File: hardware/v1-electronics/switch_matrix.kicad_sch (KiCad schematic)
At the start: 230 parts, among them SW1 MSwitch, SW10 MSwitch, SW11 MSwitch, SW12 MSwitch, SW13 MSwitch, SW14 MSwitch, SW15 MSwitch, SW16 MSwitch, SW17 MSwitch, SW18 MSwitch, SW19 MSwitch, SW2 MSwitch, SW20 MSwitch, SW21 SW_DIP_x01, SW22 SW_DIP_x01, SW23 MSwitch, SW24 MSwitch, SW25 MSwitch, SW26 MSwitch, SW27 MSwitch, SW28 MSwitch, SW29 MSwitch, SW3 MSwitch, SW30 MSwitch, SW31 MSwitch, SW32 MSwitch, SW33 MSwitch, SW34 MSwitch, SW35 SW_DIP_x01, SW36 SW_DIP_x01, SW37 MSwitch, SW38 MSwitch, SW39 MSwitch, SW4 MSwitch, SW40 MSwitch, SW41 MSwitch, SW42 MSwitch, SW43 MSwitch, SW44 MSwitch, SW45 MSwitch, SW46 MSwitch, SW47 MSwitch, SW48 MSwitch, SW49 SW_DIP_x01, SW5 MSwitch, SW50 SW_DIP_x01, SW51 MSwitch, SW52 MSwitch, SW53 MSwitch, SW54 MSwitch, SW55 MSwitch, SW56 MSwitch, SW57 MSwitch, SW58 MSwitch, SW59 MSwitch, SW6 MSwitch, SW60 MSwitch, SW61 MSwitch, SW62 MSwitch, SW63 SW_Push, SW64 SW_DIP_x01, SW65 SW_DIP_x01, SW66 SW_Push, SW67 MSwitch, SW68 MSwitch, SW69 MSwitch, SW7 SW_DIP_x01, SW70 MSwitch, SW71 MSwitch, SW72 MSwitch, SW73 SW_DIP_x01, SW74 SW_DIP_x01, SW75 SW_DIP_x01, SW76 SW_DIP_x01, SW8 SW_DIP_x01, SW9 MSwitch

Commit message: refactor(v1 hardware): root level schematic is made discriptive with hierarchical pins
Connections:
- net Column 1 renamed Column1
- net Column 10 renamed Column10
- net Column 11 renamed Column11
- net Column 12 renamed Column12
- net Column 13 renamed Column13
- net Column 14 renamed Column14
- net Column 2 renamed Column2
- net Column 3 renamed Column3
- net Column 4 renamed Column4
- net Column 5 renamed Column5
- net Column 6 renamed Column6
- net Column 7 renamed Column7
- net Column 8 renamed Column8
- net Column 9 renamed Column9
- net Row 1 renamed Row1
- net Row 2 renamed Row2
- net Row 3 renamed Row3
- net Row 4 renamed Row4
- net Row 5 renamed Row5
- net Row 6 renamed Row6

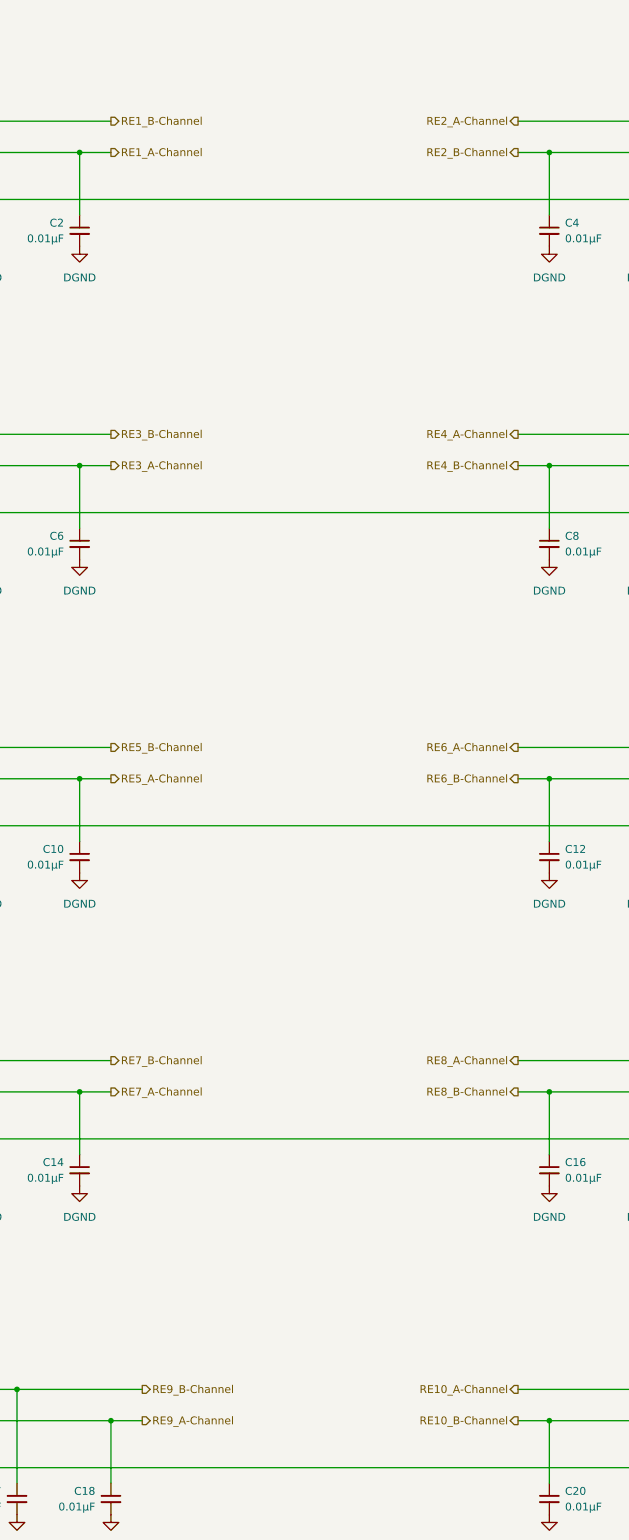
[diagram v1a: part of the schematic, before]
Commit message: refactor(v1 hardware): transition to hierarchical pins complete
All the buses renamed to stuff
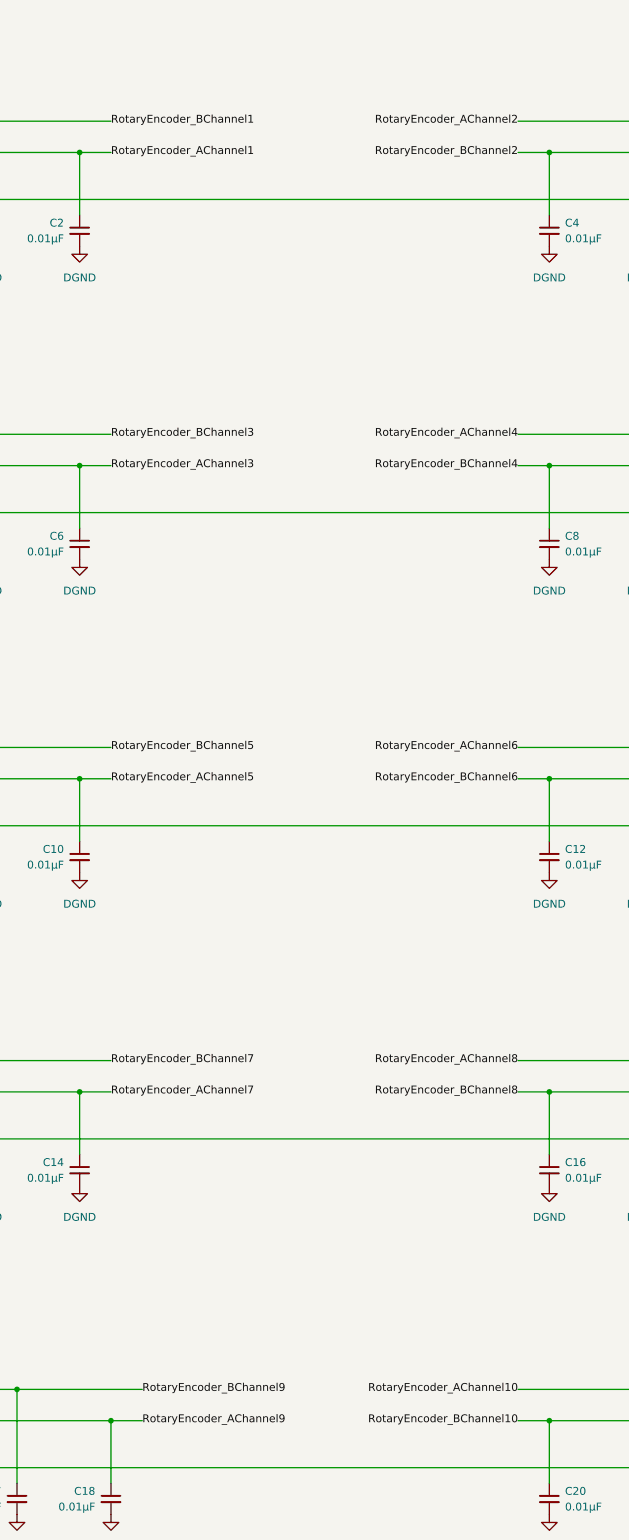
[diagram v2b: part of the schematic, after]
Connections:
- net RE10_A-Channel renamed RotaryEncoder_AChannel10
- net RE10_B-Channel renamed RotaryEncoder_BChannel10
- net RE1_A-Channel renamed RotaryEncoder_AChannel1
- net RE1_B-Channel renamed RotaryEncoder_BChannel1
- net RE2_A-Channel renamed RotaryEncoder_AChannel2
- net RE2_B-Channel renamed RotaryEncoder_BChannel2
- net RE3_A-Channel renamed RotaryEncoder_AChannel3
- net RE3_B-Channel renamed RotaryEncoder_BChannel3
- net RE4_A-Channel renamed RotaryEncoder_AChannel4
- net RE4_B-Channel renamed RotaryEncoder_BChannel4
- net RE5_A-Channel renamed RotaryEncoder_AChannel5
- net RE5_B-Channel renamed RotaryEncoder_BChannel5
- net RE6_A-Channel renamed RotaryEncoder_AChannel6
- net RE6_B-Channel renamed RotaryEncoder_BChannel6
- net RE7_A-Channel renamed RotaryEncoder_AChannel7
- net RE7_B-Channel renamed RotaryEncoder_BChannel7
- net RE8_A-Channel renamed RotaryEncoder_AChannel8
- net RE8_B-Channel renamed RotaryEncoder_BChannel8
- net RE9_A-Channel renamed RotaryEncoder_AChannel9
- net RE9_B-Channel renamed RotaryEncoder_BChannel9
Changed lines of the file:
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@@
+		)
+	)
+	(label "RotaryEncoder_AChannel4"
+		(at 299.72 88.9 180)
+		(effects
+			(font
+				(size 1.27 1.27)
+			)
+			(justify right)
 		)
 	)
@@
 		)
 	)
+	(label "RotaryEncoder_BChannel4"
+		(at 299.72 93.98 180)
+		(effects
+			(font
+				(size 1.27 1.27)
+			)
+			(justify right)
+		)
+	)
 	(label "Column7"
 		(at 203.2 304.8 90)
@@
 		)
 	)
+	(label "RotaryEncoder_AChannel2"
+		(at 299.72 38.1 180)
+		(effects
+			(font
+				(size 1.27 1.27)
+			)
+			(justify right)
+		)
+	)
 	(label "Column2"
 		(at 50.8 27.94 90)
@@
 		)
 	)
+	(label "RotaryEncoder_BChannel6"
+		(at 299.72 144.78 180)
+		(effects
+			(font
+				(size 1.27 1.27)
+			)
+			(justify right)
+		)
+	)
 	(label "Row4"
 		(at 27.94 203.2 180)
@@
 		)
 	)
+	(label "RotaryEncoder_BChannel10"
+		(at 299.72 248.92 180)
+		(effects
+			(font
+				(size 1.27 1.27)
+			)
+			(justify right)
+		)
+	)
+	(label "RotaryEncoder_AChannel3"
+		(at 233.68 93.98 0)
+		(effects
+			(font
+				(size 1.27 1.27)
+			)
+			(justify left)
+		)
+	)
+	(label "RotaryEncoder_AChannel7"
+		(at 233.68 195.58 0)
+		(effects
+			(font
+				(size 1.27 1.27)
+			)
+			(justify left)
+		)
+	)
+	(label "RotaryEncoder_BChannel8"
+		(at 299.72 195.58 180)
+		(effects
+			(font
+				(size 1.27 1.27)
+			)
+			(justify right)
+		)
+	)
 	(label "Column10"
 		(at 294.64 304.8 90)
@@
 		)
 	)
+	(label "RotaryEncoder_AChannel9"
+		(at 238.76 248.92 0)
+		(effects
+			(font
+				(size 1.27 1.27)
+			)
+			(justify left)
+		)
+	)
+	(label "RotaryEncoder_AChannel6"
+		(at 299.72 139.7 180)
+		(effects
+			(font
+				(size 1.27 1.27)
+			)
+			(justify right)
+		)
+	)
+	(label "RotaryEncoder_BChannel2"
+		(at 299.72 43.18 180)
+		(effects
+			(font
+				(size 1.27 1.27)
+			)
+			(justify right)
+		)
+	)
+	(label "RotaryEncoder_BChannel5"
+		(at 233.68 139.7 0)
+		(effects
+			(font
+				(size 1.27 1.27)
+			)
+			(justify left)
+		)
+	)
 	(label "Row1"
 		(at 27.94 50.8 180)
@@
 		)
 	)
+	(label "RotaryEncoder_BChannel3"
+		(at 233.68 88.9 0)
+		(effects
+			(font
+				(size 1.27 1.27)
+			)
+			(justify left)
+		)
+	)
 	(label "Column1"
 		(at 25.4 304.8 90)
@@
 		)
 	)
+	(label "RotaryEncoder_BChannel1"
+		(at 233.68 38.1 0)
+		(effects
+			(font
+				(size 1.27 1.27)
+			)
+			(justify left)
+		)
+	)
+	(label "RotaryEncoder_BChannel9"
+		(at 238.76 243.84 0)
+		(effects
+			(font
+				(size 1.27 1.27)
+			)
+			(justify left)
+		)
+	)
 	(label "Row6"
 		(at 25.4 314.96 180)
@@
 		)
 	)
+	(label "RotaryEncoder_AChannel8"
+		(at 299.72 190.5 180)
+		(effects
+			(font
+				(size 1.27 1.27)
+			)
+			(justify right)
+		)
+	)
+	(label "RotaryEncoder_BChannel7"
+		(at 233.68 190.5 0)
+		(effects
+			(font
+				(size 1.27 1.27)
+			)
+			(justify left)
+		)
+	)
 	(label "Column9"
 		(at 264.16 304.8 90)
@@
 		)
 	)
+	(label "RotaryEncoder_AChannel10"
+		(at 299.72 243.84 180)
+		(effects
+			(font
+				(size 1.27 1.27)
+			)
+			(justify right)
+		)
+	)
 	(label "Column7"
 		(at 139.7 27.94 90)
@@
 		)
 	)
+	(label "RotaryEncoder_AChannel1"
+		(at 233.68 43.18 0)
+		(effects
+			(font
+				(size 1.27 1.27)
+			)
+			(justify left)
+		)
+	)
+	(label "RotaryEncoder_AChannel5"
+		(at 233.68 144.78 0)
+		(effects
+			(font
+				(size 1.27 1.27)
+			)
+			(justify left)
+		)
+	)
 	(label "Row5"
 		(at 27.94 256.54 180)
@@
 			)
 			(justify left)
-		)
-	)
-	(hierarchical_label "RE4_A-Channel"
-		(shape output)
-		(at 299.72 88.9 180)
-		(effects
-			(font
-				(size 1.27 1.27)
-			)
-			(justify right)
-		)
-	)
-	(hierarchical_label "RE4_B-Channel"
-		(shape output)
-		(at 299.72 93.98 180)
-		(effects
-			(font
-				(size 1.27 1.27)
-			)
-			(justify right)
 		)
 	)
@@
 		)
 	)
-	(hierarchical_label "RE2_A-Channel"
-		(shape output)
-		(at 299.72 38.1 180)
-		(effects
-			(font
-				(size 1.27 1.27)
-			)
-			(justify right)
-		)
-	)
-	(hierarchical_label "RE6_B-Channel"
-		(shape output)
-		(at 299.72 144.78 180)
-		(effects
-			(font
-				(size 1.27 1.27)
-			)
-			(justify right)
-		)
-	)
-	(hierarchical_label "RE10_B-Channel"
-		(shape output)
-		(at 299.72 248.92 180)
-		(effects
-			(font
-				(size 1.27 1.27)
-			)
-			(justify right)
-		)
-	)
-	(hierarchical_label "RE3_A-Channel"
-		(shape output)
-		(at 233.68 93.98 0)
-		(effects
-			(font
-				(size 1.27 1.27)
-			)
-			(justify left)
-		)
-	)
-	(hierarchical_label "RE7_A-Channel"
-		(shape output)
-		(at 233.68 195.58 0)
-		(effects
-			(font
-				(size 1.27 1.27)
-			)
-			(justify left)
-		)
-	)
-	(hierarchical_label "RE8_B-Channel"
-		(shape output)
-		(at 299.72 195.58 180)
-		(effects
-			(font
-				(size 1.27 1.27)
-			)
-			(justify right)
-		)
-	)
-	(hierarchical_label "RE9_A-Channel"
-		(shape output)
-		(at 238.76 248.92 0)
-		(effects
-			(font
-				(size 1.27 1.27)
-			)
-			(justify left)
-		)
-	)
-	(hierarchical_label "RE6_A-Channel"
-		(shape output)
-		(at 299.72 139.7 180)
-		(effects
-			(font
-				(size 1.27 1.27)
-			)
-			(justify right)
-		)
-	)
-	(hierarchical_label "RE2_B-Channel"
-		(shape output)
-		(at 299.72 43.18 180)
-		(effects
-			(font
-				(size 1.27 1.27)
-			)
-			(justify right)
-		)
-	)
-	(hierarchical_label "RE5_B-Channel"
-		(shape output)
-		(at 233.68 139.7 0)
-		(effects
-			(font
-				(size 1.27 1.27)
-			)
-			(justify left)
-		)
-	)
-	(hierarchical_label "RE3_B-Channel"
-		(shape output)
-		(at 233.68 88.9 0)
-		(effects
-			(font
-				(size 1.27 1.27)
-			)
-			(justify left)
-		)
-	)
-	(hierarchical_label "RE1_B-Channel"
-		(shape output)
-		(at 233.68 38.1 0)
-		(effects
-			(font
-				(size 1.27 1.27)
-			)
-			(justify left)
-		)
-	)
-	(hierarchical_label "RE9_B-Channel"
-		(shape output)
-		(at 238.76 243.84 0)
-		(effects
-			(font
-				(size 1.27 1.27)
-			)
-			(justify left)
-		)
-	)
-	(hierarchical_label "RE8_A-Channel"
-		(shape output)
-		(at 299.72 190.5 180)
-		(effects
-			(font
-				(size 1.27 1.27)
-			)
-			(justify right)
-		)
-	)
-	(hierarchical_label "RE7_B-Channel"
-		(shape output)
-		(at 233.68 190.5 0)
-		(effects
-			(font
-				(size 1.27 1.27)
-			)
-			(justify left)
-		)
-	)
 	(hierarchical_label "RotaryEncoder_AChannel[1..10]"
 		(shape output)
@@
 		(effects
 			(font
-				(size 1.27 1.27)
-			)
-			(justify left)
-		)
-	)
-	(hierarchical_label "RE10_A-Channel"
-		(shape output)
-		(at 299.72 243.84 180)
-		(effects
-			(font
-				(size 1.27 1.27)
-			)
-			(justify right)
-		)
-	)
-	(hierarchical_label "RE1_A-Channel"
-		(shape output)
-		(at 233.68 43.18 0)
-		(effects
-			(font
-				(size 1.27 1.27)
-			)
-			(justify left)
-		)
-	)
-	(hierarchical_label "RE5_A-Channel"
-		(shape output)
-		(at 233.68 144.78 0)
-		(effects
-			(font

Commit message: refactor(v1 hardware): get references in order
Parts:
- renumbered D71 to D73, D72 to D74, D73 to D75, D74 to D76, D75 to D77, D77 to D85, SW7 to SW73, SW8 to SW74, SW21 to SW75, SW22 to SW76, SW35 to SW77, SW36 to SW78, SW49 to SW79, SW50 to SW80, SW64 to SW81, SW65 to SW82, SW73 to SW83, SW74 to SW84, SW75 to SW85, SW76 to SW86
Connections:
- net at D78.2 (A): now also SW78.2; no longer SW80.2
- net at D85.2 (A): now also SW85.2; no longer SW79.2
- net at SW83.2: now also D83.2 (A); no longer D81.2 (A)
- net at SW82.2: now also D82.2 (A); no longer D80.2 (A)
- net at D79.2 (A): now also SW79.2; no longer SW81.2
- net at SW86.2: now also D76.2 (A); no longer D84.2 (A)
- net at SW84.2: now also D84.2 (A); no longer D82.2 (A)
- new net: D81.2 (A), SW81.2
- new net: D80.2 (A), SW80.2
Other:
- moved on the sheet: D76, D78, D79, D80, D81, D82, D83, D84, D85
